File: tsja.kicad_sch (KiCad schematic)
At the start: 69 parts, among them J1 QWIIC, J2 Micro_SD_Card, J3 SAO, J4 EXT, J6 USB-C, M1 Vibration, Q1 AP2302B, Q4 AO3400 (A09T), Q5 AO3400 (A09T), T1 Select, T2 Start, T3 B, T4 A, T5 Cross, U1 74LVC1G17GW,125, U10 SY6280AAC, U11 SK6805, U12 SK6805, U13 SK6805, U14 SK6805, U15 SK6805, U2 MPR121QR2, U3 ESP32-WROVER-E, U7 CH340K, U8 SK6805, U9 SY6280AAC

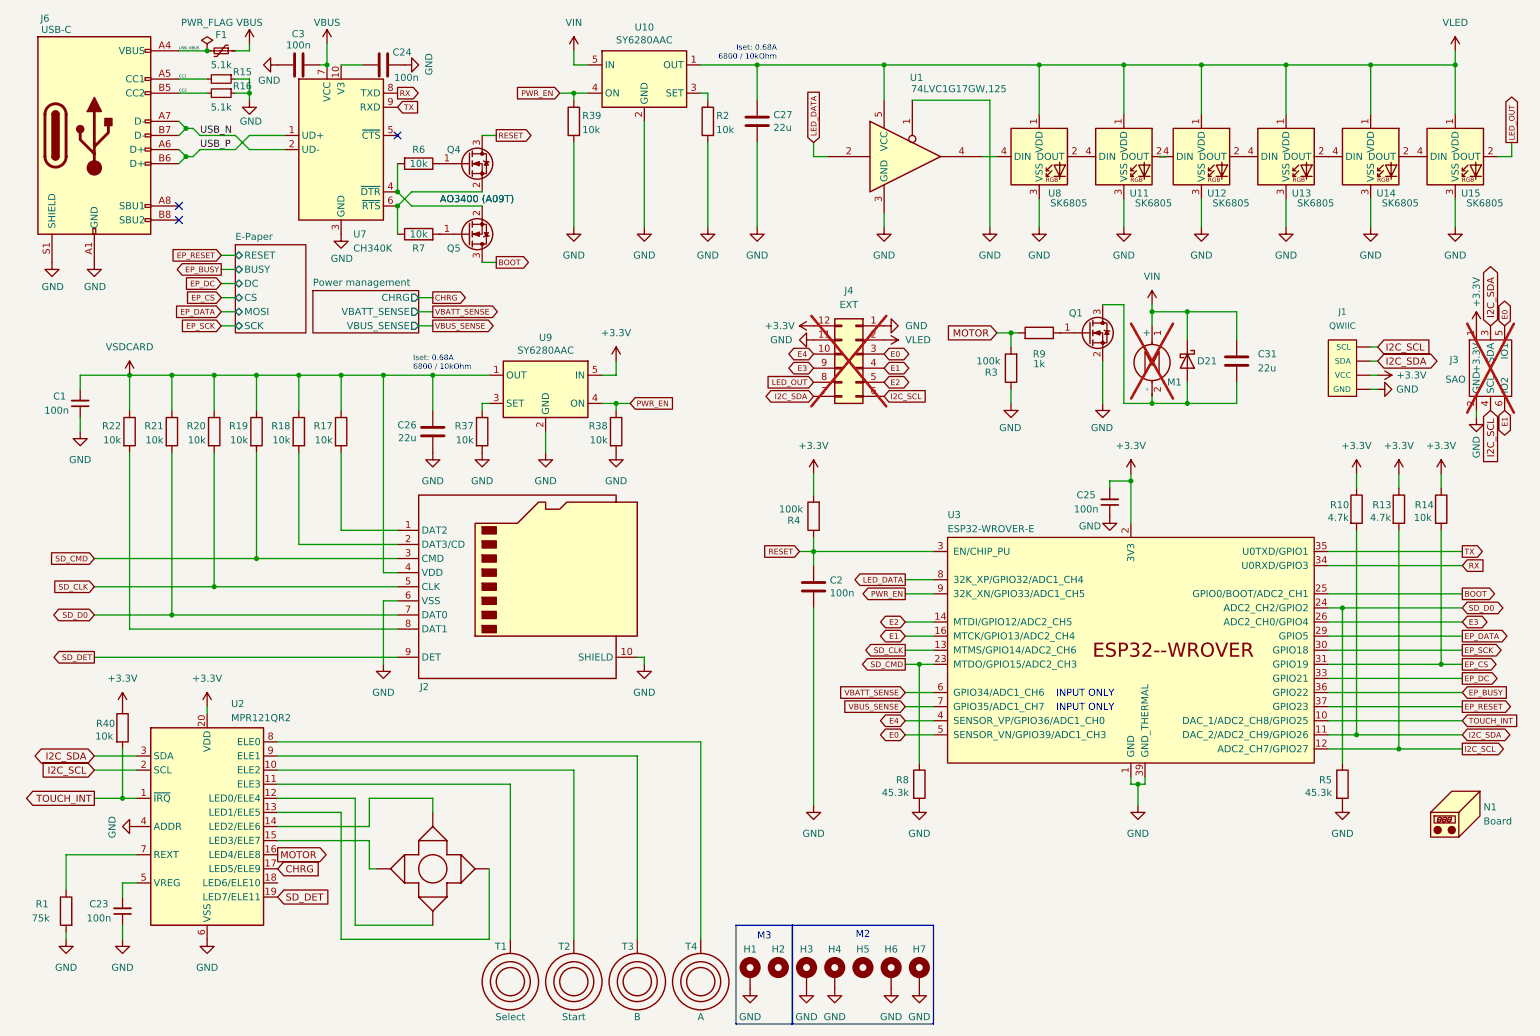
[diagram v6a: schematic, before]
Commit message: Route captouch traces through inner layer, add two buttons, remove vibration motor
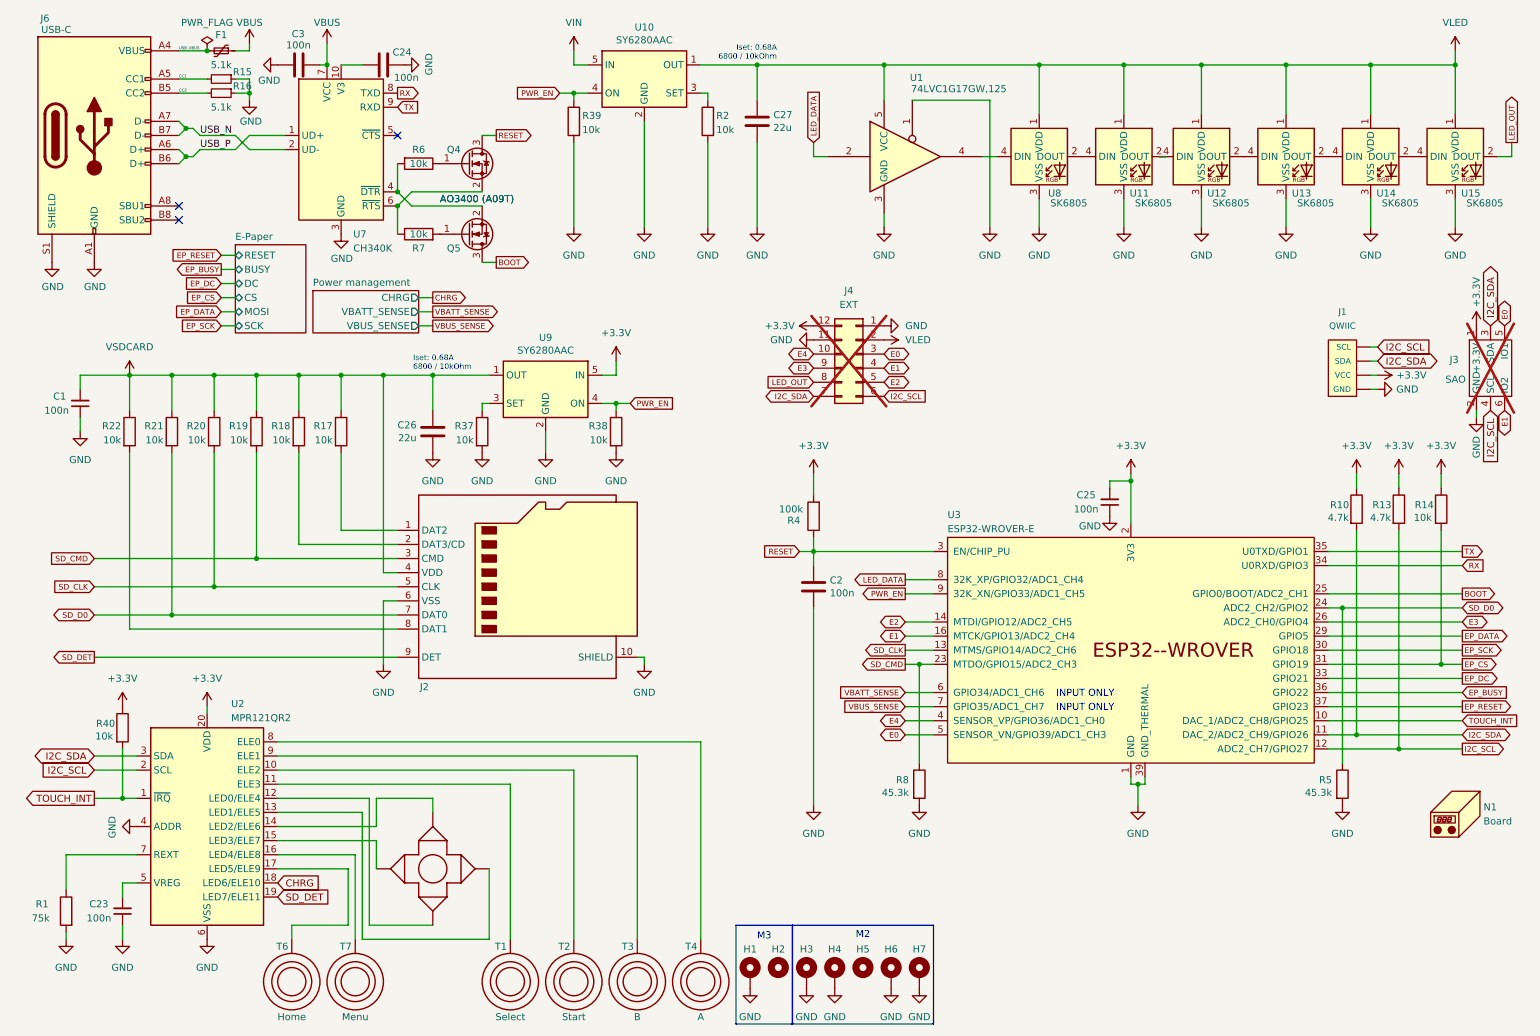
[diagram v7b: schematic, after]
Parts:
- removed C31: 22u, Capacitor_SMD:C_0805_2012Metric, symbol Device:C
- removed D21: NSR0320MW2T1G, library:D_SOD-323, symbol symbols:D_Schottky
- removed M1: Vibration, Connector_PinHeader_2.54mm:PinHeader_1x02_P2.54mm_Vertical_SMD_Pin1Left, symbol Motor:Motor_DC
- removed Q1: AP2302B, library:SOT-23, symbol symbols:Q_NMOS_GSD
- removed R3: 100k, Resistor_SMD:R_0402_1005Metric, symbol symbols:R
- removed R9: 1k, Resistor_SMD:R_0402_1005Metric, symbol symbols:R
- added T6: Home, design:home, symbol library:TOUCHSELECT
- added T7: Menu, design:menu, symbol library:TOUCHSELECT
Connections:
- net CHRG: now also U2.18 (LED6/ELE10); no longer U2.17 (LED5/ELE9)
- net MOTOR: no longer names the net of U2.16 (LED4/ELE8)
- net MOTOR: now also T7.1
- new net: T6.1, U2.17 (LED5/ELE9)
